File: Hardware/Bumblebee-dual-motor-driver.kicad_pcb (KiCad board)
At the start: 2 copper layers, 83 parts, among them J1 ICSP, J10 GND, J11 MOTOR1_A, J12 MOTOR1_B, J13 MOTOR2_A, J14 MOTOR2_B, J15 MAIN+, J16 MAIN-, J2 USB_B_Micro, J3 HEADER, J4 HEADER, J5 JST-PH, J6 JST-PH, J7 12V_OUT, J8 5V_OUT, J9 GND, Q1 Q_NMOS_DGS, Q2 Q_NMOS_DGS, Q3 Q_NMOS_DGS, Q4 Q_NMOS_DGS, Q5 Q_NMOS_DGS, Q6 Q_NMOS_DGS, Q7 Q_NMOS_DGS, Q8 Q_NMOS_DGS, SW1 SW_DIP_x04, U1 ATmega328P-AU, U2 FT232RL, U3 74LS08, U4 74LVC2G240, U5 R-78E5.0-0.5, U6 A4940KLPTR-T, U7 A4940KLPTR-T

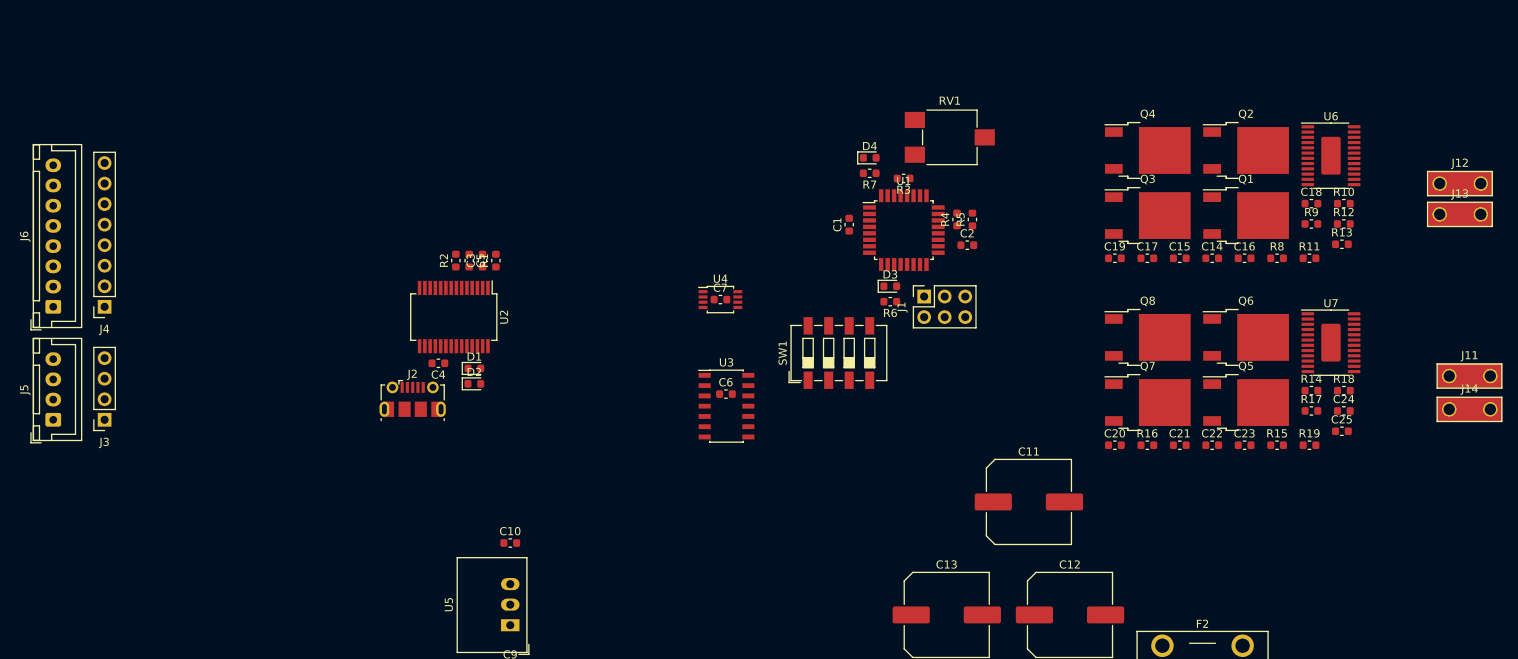
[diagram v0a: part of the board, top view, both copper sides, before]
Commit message: Fixed small issues and started laying out H-bridge
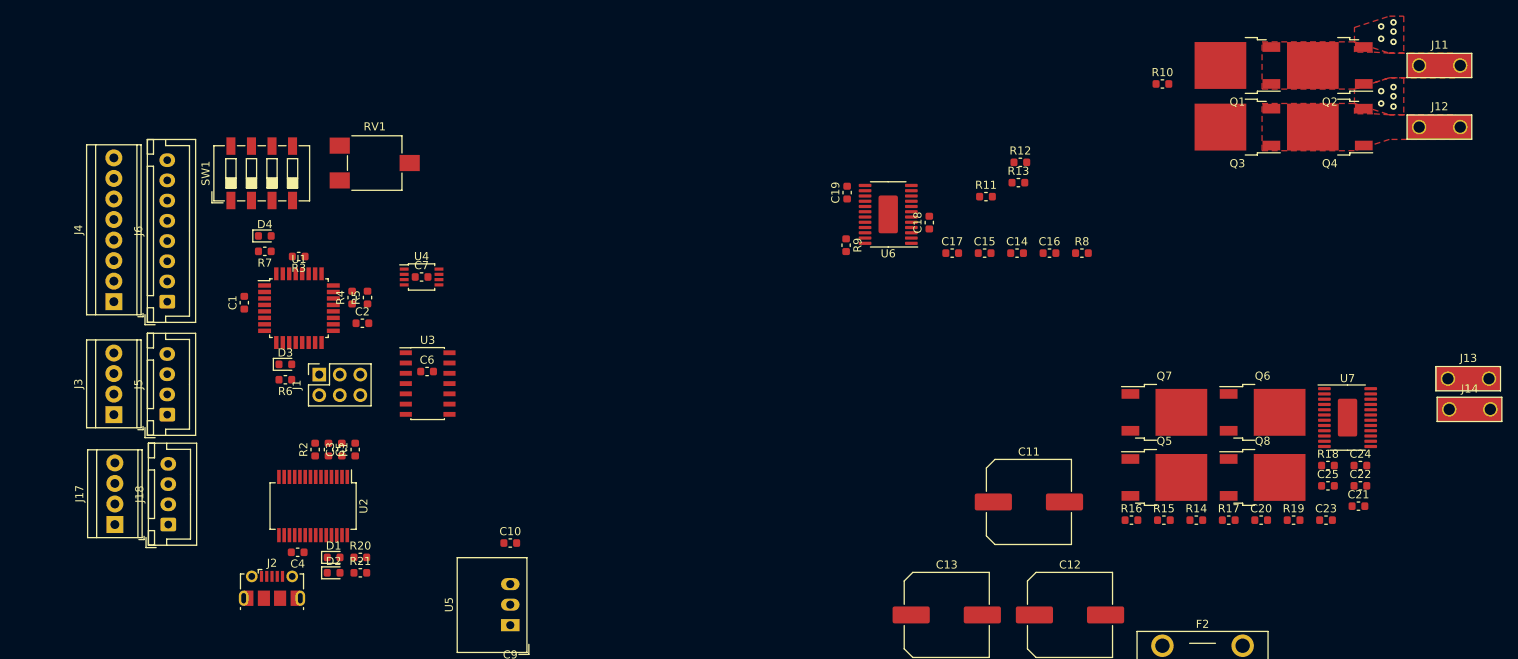
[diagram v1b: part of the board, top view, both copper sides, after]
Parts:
- added J17: HEADER, TerminalBlock_TE-Connectivity:TerminalBlock_TE_282834-4_1x04_P2.54mm_Horizontal, F.Cu at (76.2, 126.0)
- added J18: JST-XH, Connector_JST:JST_XH_B4B-XH-A_1x04_P2.50mm_Vertical, F.Cu at (82.8, 126.0)
- added R20: 1k, Resistor_SMD:R_0603_1608Metric, F.Cu at (106.6, 130.0)
- added R21: 1k, Resistor_SMD:R_0603_1608Metric, F.Cu at (106.6, 132.0)
- J3: footprint Connector_PinSocket_2.54mm:PinSocket_1x04_P2.54mm_Vertical -> TerminalBlock_TE-Connectivity:TerminalBlock_TE_282834-4_1x04_P2.54mm_Horizontal
- J4: footprint Connector_PinSocket_2.54mm:PinSocket_1x08_P2.54mm_Vertical -> TerminalBlock_TE-Connectivity:TerminalBlock_TE_282834-8_1x08_P2.54mm_Horizontal
- J5, J6: value JST-PH -> JST-XH
- Q1, Q2, Q3, Q4, Q5, Q6, Q7, Q8: value Q_NMOS_DGS -> Q_NMOS_GDS
- moved C2 75.4 mm to (106.8, 101.1)
- moved D3 75.4 mm to (97.3, 106.2)
- moved J1 75.4 mm to (101.5, 107.4)
- moved R5 75.4 mm to (107.4, 97.9)
- moved R6 75.4 mm to (97.3, 108.1)
- moved U1 75.4 mm to (99.0, 99.2)
- moved C1 75.4 mm to (92.2, 98.6)
- moved R4 75.4 mm to (105.5, 97.9)
- moved D4 75.4 mm to (94.7, 90.3)
- moved R3 75.4 mm to (98.9, 92.8)
- moved R7 75.4 mm to (94.7, 92.2)
- moved SW1 74.8 mm to (94.4, 82.5)
- moved RV1 71.2 mm to (108.3, 81.3)
- moved R9 57.6 mm to (166.6, 91.4), turned to 270 degrees
- moved U6 55.2 mm to (171.8, 87.6), turned to 180 degrees
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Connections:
- C17 pad 1: /MOTOR1_DRIVER/MOTOR_A -> /MOTOR1_A
- C18 pad 1: /MOTOR1_DRIVER/MOTOR_B -> /MOTOR1_B
- C23 pad 1: /MOTOR2_DRIVER/MOTOR_A -> /MOTOR2_A
- C24 pad 1: /MOTOR2_DRIVER/MOTOR_B -> /MOTOR2_B
- D1 pad 2: VCC -> Net-(D1-Pad2)
- D2 pad 2: VCC -> Net-(D2-Pad2)
- J11 pad 1: /MOTOR1_DRIVER/MOTOR_A -> /MOTOR1_A
- J12 pad 1: /MOTOR1_DRIVER/MOTOR_B -> /MOTOR1_B
- J13 pad 1: /MOTOR2_DRIVER/MOTOR_A -> /MOTOR2_A
- J14 pad 1: /MOTOR2_DRIVER/MOTOR_B -> /MOTOR2_B
- Q1 pad 1: VBUS -> Net-(Q1-Pad1)
- Q1 pad 2: Net-(Q1-Pad2) -> VBUS
- Q1 pad 3: /MOTOR1_DRIVER/MOTOR_A -> /MOTOR1_A
- Q2 pad 1: /MOTOR1_DRIVER/MOTOR_A -> Net-(Q2-Pad1)
- Q2 pad 2: Net-(Q2-Pad2) -> /MOTOR1_A
- Q3 pad 1: VBUS -> Net-(Q3-Pad1)
- Q3 pad 2: Net-(Q3-Pad2) -> VBUS
- Q3 pad 3: /MOTOR1_DRIVER/MOTOR_B -> /MOTOR1_B
- Q4 pad 1: /MOTOR1_DRIVER/MOTOR_B -> Net-(Q4-Pad1)
- Q4 pad 2: Net-(Q4-Pad2) -> /MOTOR1_B
- Q5 pad 1: VBUS -> Net-(Q5-Pad1)
- Q5 pad 2: Net-(Q5-Pad2) -> VBUS
- Q5 pad 3: /MOTOR2_DRIVER/MOTOR_A -> /MOTOR2_A
- Q6 pad 1: /MOTOR2_DRIVER/MOTOR_A -> Net-(Q6-Pad1)
- Q6 pad 2: Net-(Q6-Pad2) -> /MOTOR2_A
- Q7 pad 1: VBUS -> Net-(Q7-Pad1)
- Q7 pad 2: Net-(Q7-Pad2) -> VBUS
- Q7 pad 3: /MOTOR2_DRIVER/MOTOR_B -> /MOTOR2_B
- Q8 pad 1: /MOTOR2_DRIVER/MOTOR_B -> Net-(Q8-Pad1)
- Q8 pad 2: Net-(Q8-Pad2) -> /MOTOR2_B
- R10 pad 1: Net-(Q1-Pad2) -> Net-(Q1-Pad1)
- R11 pad 1: Net-(Q2-Pad2) -> Net-(Q2-Pad1)
- R12 pad 1: Net-(Q3-Pad2) -> Net-(Q3-Pad1)
- R13 pad 1: Net-(Q4-Pad2) -> Net-(Q4-Pad1)
- R16 pad 1: Net-(Q5-Pad2) -> Net-(Q5-Pad1)
- R17 pad 1: Net-(Q6-Pad2) -> Net-(Q6-Pad1)
- R18 pad 1: Net-(Q7-Pad2) -> Net-(Q7-Pad1)
- R19 pad 1: Net-(Q8-Pad2) -> Net-(Q8-Pad1)
- U2 pad 10: Net-(U2-Pad10) -> (no net)
- U2 pad 11: Net-(U2-Pad11) -> (no net)
- U2 pad 12: Net-(U2-Pad12) -> (no net)
- U2 pad 13: Net-(U2-Pad13) -> (no net)
- U2 pad 14: Net-(U2-Pad14) -> (no net)
- U2 pad 27: Net-(U2-Pad27) -> (no net)
- U2 pad 28: Net-(U2-Pad28) -> (no net)
- U2 pad 3: Net-(U2-Pad3) -> (no net)
- U2 pad 6: Net-(U2-Pad6) -> (no net)
- U2 pad 9: Net-(U2-Pad9) -> (no net)
- U4 pad 1: Net-(U4-Pad1) -> (no net)
- U4 pad 7: Net-(U4-Pad7) -> (no net)
- U6 pad 1: /MOTOR1_DRIVER/~RESET -> (no net)
- U6 pad 10: /MOTOR1_DRIVER/MOTOR_A -> /MOTOR1_A
- U6 pad 4: /MOTOR1_DRIVER/MOTOR_B -> /MOTOR1_B
- U7 pad 1: /MOTOR2_DRIVER/~RESET -> (no net)
- U7 pad 10: /MOTOR2_DRIVER/MOTOR_A -> /MOTOR2_A
- U7 pad 4: /MOTOR2_DRIVER/MOTOR_B -> /MOTOR2_B
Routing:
- net GND: vias 0 -> 10
- added copper zone on F.Cu, net /MOTOR1_A
- added copper zone on F.Cu, net /MOTOR1_B
- added copper zone on F.Cu, net GND
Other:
- net class Default: clearance 0.2 -> 0.1524; trace_width 0.25 -> 0.1524
- rule trace_clearance: 0.2 -> 0.1524
- rule trace_min: 0.2 -> 0.1524

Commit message: Layed out single H-bridge, started copying to the other H-bridge
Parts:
- removed the C14 at (187.8, 92.4)
- removed the C15 at (183.8, 92.4)
- removed the C16 at (191.8, 92.4)
- removed the C17 at (179.7, 92.4)
- removed the C18 at (176.9, 88.6)
- removed the C19 at (166.8, 84.9)
- removed the R10 at (205.7, 71.5)
- removed the R11 at (183.9, 85.4)
- removed the R12 at (188.2, 81.2)
- removed the R13 at (187.9, 83.7)
- removed the R8 at (195.8, 92.4)
- removed the R9 at (166.6, 91.4)
- added C14: 0.1u, Capacitor_SMD:C_0603_1608Metric, F.Cu at (251.6, 82.7)
- added C14: 0.1u, Capacitor_SMD:C_0603_1608Metric, F.Cu at (203.5, 82.8)
- added C15: 10u, Capacitor_SMD:C_0603_1608Metric, F.Cu at (253.0, 70.2)
- added C15: 10u, Capacitor_SMD:C_0603_1608Metric, F.Cu at (204.9, 70.4)
- added C16: 0.1u, Capacitor_SMD:C_0603_1608Metric, F.Cu at (247.3, 74.5)
- added C16: 0.1u, Capacitor_SMD:C_0603_1608Metric, F.Cu at (199.1, 74.7)
- added C17: 1u, Capacitor_SMD:C_0603_1608Metric, F.Cu at (250.7, 71.9)
- added C17: 1u, Capacitor_SMD:C_0603_1608Metric, F.Cu at (202.6, 72.0)
- added C18: 1u, Capacitor_SMD:C_0603_1608Metric, F.Cu at (253.7, 71.9)
- added C18: 1u, Capacitor_SMD:C_0603_1608Metric, F.Cu at (205.6, 72.0)
- added C19: 1u, Capacitor_SMD:C_0603_1608Metric, F.Cu at (247.3, 79.6)
- added C19: 1u, Capacitor_SMD:C_0603_1608Metric, F.Cu at (199.1, 79.8)
- added J11: MOTOR1_A, TE_1217861-1:TE_1217861-1, F.Cu at (285.6, 69.1)
- added J12: MOTOR1_B, TE_1217861-1:TE_1217861-1, F.Cu at (285.6, 76.7)
- added R10: 27, Resistor_SMD:R_0603_1608Metric, F.Cu at (249.8, 70.2)
- added R10: 27, Resistor_SMD:R_0603_1608Metric, F.Cu at (201.7, 70.4)
- added R11: 27, Resistor_SMD:R_0603_1608Metric, F.Cu at (251.6, 68.3)
- added R11: 27, Resistor_SMD:R_0603_1608Metric, F.Cu at (203.5, 68.5)
- added R12: 27, Resistor_SMD:R_0603_1608Metric, F.Cu at (255.8, 68.3)
- added R12: 27, Resistor_SMD:R_0603_1608Metric, F.Cu at (207.6, 68.5)
- added R13: 27, Resistor_SMD:R_0603_1608Metric, F.Cu at (256.4, 70.9)
- added R13: 27, Resistor_SMD:R_0603_1608Metric, F.Cu at (208.3, 71.0)
- added R8: 10k, Resistor_SMD:R_0603_1608Metric, F.Cu at (256.4, 82.7)
- added R8: 10k, Resistor_SMD:R_0603_1608Metric, F.Cu at (208.3, 82.8)
- added R9: 82k, Resistor_SMD:R_0603_1608Metric, F.Cu at (254.8, 82.7)
- added R9: 82k, Resistor_SMD:R_0603_1608Metric, F.Cu at (206.6, 82.8)
- moved C21 109.5 mm to (330.2, 79.5)
- moved J13 109.5 mm to (341.2, 63.8)
- moved R15 109.5 mm to (306.1, 81.2)
- moved C20 109.5 mm to (318.2, 81.2)
- moved J14 109.5 mm to (341.4, 67.5)
- moved R14 109.5 mm to (310.1, 81.2)
- moved R17 109.5 mm to (314.1, 81.2)
- moved C22 109.5 mm to (330.4, 77.0)
- moved C23 109.5 mm to (326.2, 81.2)
- moved C24 109.5 mm to (330.4, 74.5)
- moved C25 109.5 mm to (326.4, 77.0)
- moved R16 109.5 mm to (302.1, 81.2)
- moved R18 109.5 mm to (326.4, 74.5)
- moved R19 109.5 mm to (322.2, 81.2)
- moved Q5 71.8 mm to (263.1, 76.7), turned to 180 degrees
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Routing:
- net (no net): track 0.00 -> 246.1 mm, vias 0 -> 19
- net Net-(Q2-Pad1): track 0.00 -> 34.3 mm
- net Net-(Q4-Pad1): track 0.00 -> 27.6 mm, vias 0 -> 2
- net /MOTOR1_B: track 0.00 -> 27.3 mm
- net Net-(Q1-Pad1): track 0.00 -> 26.4 mm
- net /MOTOR1_A: track 0.00 -> 25.8 mm, vias 0 -> 2
- net GND: track 0.00 -> 24.5 mm, vias 10 -> 29
- net Net-(Q3-Pad1): track 0.00 -> 23.9 mm
- net VBUS: track 0.00 -> 18.9 mm, vias 0 -> 2
- net +5V: track 0.00 -> 9.51 mm
- net Net-(R11-Pad2): track 0.00 -> 8.14 mm
- net Net-(R12-Pad2): track 0.00 -> 6.41 mm
- net Net-(R13-Pad2): track 0.00 -> 4.71 mm
- net Net-(R10-Pad2): track 0.00 -> 3.97 mm
- net Net-(C15-Pad1): track 0.00 -> 3.89 mm
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- added copper zone on F.Cu, net /MOTOR2_A
- added copper zone on F.Cu, net /MOTOR2_B
- added copper zone on B.Cu, net GND
- added copper zone on F.Cu, net VBUS

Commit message: Further progress laying out Bumblebee
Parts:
- removed the C14 at (251.6, 82.7)
- removed the C15 at (253.0, 70.2)
- removed the C16 at (247.3, 74.5)
- removed the C17 at (250.7, 71.9)
- removed the C18 at (253.7, 71.9)
- removed the C19 at (247.3, 79.6)
- removed the J11 at (285.6, 69.1)
- removed the J12 at (285.6, 76.7)
- removed the R10 at (249.8, 70.2)
- removed the R11 at (251.6, 68.3)
- removed the R12 at (255.8, 68.3)
- removed the R13 at (256.4, 70.9)
- removed the R8 at (256.4, 82.7)
- removed the R9 at (254.8, 82.7)
- removed the R9 at (206.6, 82.8)
- added R9: 82k, Resistor_SMD:R_0603_1608Metric, F.Cu at (132.6, 98.9)
- moved C22 208.0 mm to (125.1, 110.4), turned to 90 degrees
- moved C25 205.0 mm to (125.1, 115.4), turned to 90 degrees
- moved C24 201.6 mm to (131.6, 107.7), turned to 180 degrees
- moved C21 201.1 mm to (130.8, 106.0)
- moved C23 199.4 mm to (128.5, 107.7)
- moved R18 195.1 mm to (133.6, 104.1), turned to 180 degrees
- moved C20 191.8 mm to (130.2, 119.3)
- moved R19 189.6 mm to (134.2, 106.7), turned to 90 degrees
- moved R17 186.1 mm to (129.4, 104.1), turned to 180 degrees
- moved J14 183.6 mm to (163.4, 112.5)
- moved J13 182.5 mm to (163.4, 104.9)
- moved R14 179.8 mm to (134.2, 118.5), turned to 90 degrees
- moved R15 177.5 mm to (132.6, 118.5), turned to 270 degrees
- moved R16 176.2 mm to (127.6, 106.0)
- moved Q7 129.6 mm to (141.0, 112.5)
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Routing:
- net (no net): track 246.1 -> 0.00 mm, vias 19 -> 0
- net Net-(Q8-Pad1): track 0.00 -> 66.5 mm, vias 0 -> 2
- net Net-(Q6-Pad1): track 0.00 -> 34.3 mm
- net /MOTOR2_A: track 0.00 -> 33.1 mm, vias 0 -> 2
- net VBUS: track 18.9 -> 49.5 mm, vias 2 -> 11
- net /MOTOR2_B: track 0.00 -> 27.3 mm
- net Net-(Q5-Pad1): track 0.00 -> 26.4 mm
- net +5V: track 9.51 -> 33.5 mm
- net Net-(Q7-Pad1): track 0.00 -> 23.9 mm
- net Net-(F1-Pad2): track 0.00 -> 13.4 mm
- net GND: track 24.5 -> 33.4 mm, vias 29 -> 66
- net Net-(R17-Pad2): track 0.00 -> 8.14 mm
- net Net-(R18-Pad2): track 0.00 -> 6.41 mm
- net Net-(R19-Pad2): track 0.00 -> 4.71 mm
- net Net-(R16-Pad2): track 0.00 -> 3.97 mm
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- added copper zone on F.Cu, net Net-(F2-Pad2)
- added copper zone on B.Cu, net VBUS

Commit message: Finished routing board. Need to still do documentation.
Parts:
- added G***: LOGO, logo:bumblebee_logo, B.Cu at (98.3, 135.4)
- added G***: LOGO, logo:bumblebee_logo, F.Cu at (103.4, 144.5)
- added REF**: MountingHole_3.2mm_M3, MountingHole:MountingHole_3.2mm_M3, F.Cu at (104.9, 81.9)
- added REF**: MountingHole_3.2mm_M3, MountingHole:MountingHole_3.2mm_M3, F.Cu at (83.3, 149.9)
- added REF**: MountingHole_3.2mm_M3, MountingHole:MountingHole_3.2mm_M3, F.Cu at (167.3, 138.9)
- added REF**: MountingHole_3.2mm_M3, MountingHole:MountingHole_3.2mm_M3, F.Cu at (167.3, 80.9)
- J1: footprint Connector_PinSocket_2.54mm:PinSocket_2x03_P2.54mm_Vertical -> Connector_PinHeader_2.54mm:PinHeader_2x03_P2.54mm_Vertical
- moved R3 42.2 mm to (112.6, 132.7), turned to 90 degrees
- moved RV1 41.3 mm to (106.7, 122.6), turned to 90 degrees
- moved R6 28.8 mm to (121.3, 92.1)
- moved R7 27.9 mm to (118.6, 106.7), turned to 270 degrees
- moved D4 27.5 mm to (116.8, 106.7), turned to 90 degrees
- moved D3 27.0 mm to (121.3, 93.9)
- moved C5 22.0 mm to (87.1, 132.3), turned to 90 degrees
- moved SW1 20.2 mm to (114.6, 83.2)
- moved C7 18.8 mm to (120.7, 113.0)
- moved U4 18.8 mm to (115.8, 114.0)
- moved C3 16.3 mm to (110.1, 132.0), turned to 0 degrees
- moved R2 16.1 mm to (106.0, 132.0), turned to 0 degrees
- moved R1 15.5 mm to (102.9, 132.0), turned to 0 degrees
- moved U1 15.0 mm to (113.9, 99.2), turned to 180 degrees
- moved C4 14.3 mm to (89.7, 140.5), turned to 0 degrees
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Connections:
- C5 pad 1: VCC -> /USB_PWR
- J2 pad 1: VCC -> /USB_PWR
- R20 pad 2: VCC -> +5V
- R21 pad 2: VCC -> +5V
- U1 pad 12: Net-(SW1-Pad1) -> Net-(SW1-Pad3)
- U1 pad 14: Net-(SW1-Pad3) -> Net-(SW1-Pad1)
- U1 pad 19: /JS_X -> /JS_Y
- U1 pad 22: /JS_Y -> /JS_X
- U1 pad 24: /NTC1 -> /NTC2
- U1 pad 25: /NTC2 -> /NTC1
- U2 pad 19: VCC -> +5V
- U2 pad 20: VCC -> /USB_PWR
- U2 pad 4: VCC -> /USB_PWR
- U4 pad 8: VCC -> +5V
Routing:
- net +5V: track 33.5 -> 265.9 mm, vias 0 -> 5
- net /BTN_R: track 0.00 -> 46.5 mm, vias 0 -> 1
- net /NTC1: track 0.00 -> 46.4 mm
- net /NTC2: track 0.00 -> 45.3 mm
- net /BTN_UP: track 0.00 -> 41.7 mm, vias 0 -> 1
- net /RESET: track 0.00 -> 41.3 mm, vias 0 -> 2
- net /BTN_L: track 0.00 -> 40.6 mm, vias 0 -> 1
- net /JS_Y: track 0.00 -> 40.3 mm, vias 0 -> 1
- net /M8RXD: track 0.00 -> 38.8 mm, vias 0 -> 2
- net /MOTOR1_DRIVER/AHI: track 3.85 -> 42.1 mm
- net /JS_X: track 0.00 -> 37.4 mm, vias 0 -> 1
- net GND: track 33.4 -> 70.5 mm, vias 66 -> 114
- net /MOTOR1_DRIVER/ALO: track 0.65 -> 36.9 mm
- net /M8TXD: track 0.00 -> 34.9 mm, vias 0 -> 2
- net /MOTOR1_DIR: track 0.00 -> 32.9 mm, vias 0 -> 2
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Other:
- board outline added: 91.8 x 75.9 mm
- net class Default: via_dia 0.8 -> 0.6; via_drill 0.4 -> 0.3
- rule via_min_size: 0.4 -> 0.6
- board text added: "1 2"
- board text added: "BUTTONS"
- board text added: "BumbleBee"
- board text added: "CONFIG"
- board text added: "Dual-motor control board"
- board text added: "GND L/R F/RV 5V"
- board text added: "JOYSTICK"
- board text added: "R L REV FOR"
- board text added: "SPEED"
- board text added: "TEMPS"
- board text added: "USB"
- board text added: "Willem Hillier revA 5/9/2019"

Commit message: Done with silkscreen
TODO: Add keepout areas on high-current traces
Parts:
- added SW1: SW_DIP_x04, logo:dipLOGO, B.Cu at (146.2, 87.1)
- F1, F2: footprint Fuse:Fuseholder_Blade_Mini_Keystone_3568 -> footprints:Fuseholder_Blade_Mini_Keystone_3568
- J17, J3: footprint TerminalBlock_TE-Connectivity:TerminalBlock_TE_282834-4_1x04_P2.54mm_Horizontal -> footprints:TerminalBlock_TE_282834-4_1x04_P2.54mm_Horizontal
- J2: footprint Connector_USB:USB_Micro-B_Molex-105017-0001 -> footprints:USB_Micro-B_Molex-105017-0001
- J4: footprint TerminalBlock_TE-Connectivity:TerminalBlock_TE_282834-8_1x08_P2.54mm_Horizontal -> footprints:TerminalBlock_TE_282834-8_1x08_P2.54mm_Horizontal
- RV1: footprint Potentiometer_SMD:Potentiometer_ACP_CA6-VSMD_Vertical -> footprints:Potentiometer_Bourns_PTV09A-1_Single_Vertical
- moved REF** 17.4 mm to (153.2, 149.2)
- moved RV1 5.57 mm to (107.0, 128.1)
- moved J7 1.78 mm to (148.0, 152.4)
- moved J8 1.14 mm to (139.7, 152.4)
- moved J15 0.76 mm to (159.4, 147.3)
- moved J10 0.51 mm to (131.4, 152.4)
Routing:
- net Net-(RV1-Pad2): track 18.5 -> 28.9 mm
- net Net-(Q8-Pad1): track 50.9 -> 57.3 mm
- net +5V: track 265.9 -> 272.4 mm
- net GND: track 70.5 -> 75.6 mm, vias 114 -> 113
- net Net-(Q4-Pad1): track 27.6 -> 30.5 mm
- net (no net): vias 0 -> 1
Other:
- board text added: "+IN"
- board text added: "+OUT"
- board text added: "-Control Input Selection Up: Use buttons for input Down: Use joystick for input -Joystick X-Axis Direction -Joystick Y-Axis Direction -Check manual"
- board text added: "-GND"
- board text added: "0.5A MAX"
- board text added: "20A MAX"
- board text added: "5V_OUT"
- board text added: "CONFIG Switch Instructions"
- board text added: "NOTES: -Fuse type is mini-blade, available at most automotive stores. -Either stripped bare wires can be used on the terminal blocks, or JST XH connectors can be plugged in to the white connectors, which are more durable. -This board is 100% Arduino-compatible, and programmable as an Arduino Uno. Check manual for more information, including pin equivalencies and how to control motors. -The high-c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"
- board text added: "OUT1"
- board text added: "OUT2"
- board text added: "Switches from left to right:"
